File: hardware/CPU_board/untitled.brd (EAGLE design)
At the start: 128.9 x 94.9 mm, 67 parts, among them IC1 MAX232ECWE, IC2 MAX232ECWE, IC3 AM29F040J, IC4 74HCT138D, IC5 LM2596S, IC6 74245SSOP, IC7 74245SSOP, IC8 74245SSOP, J2 POWER_JACKSLT, U1 AS6C4008-55SIN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

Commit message: Power trace updated
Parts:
- moved IC6 1.91 mm to (54.1, 53.3)
- moved C1 1.30 mm to (51.1, 23.5)
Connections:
- removed net VCC: IC7.20, IC8.20
- net 5V: now also IC7.20, IC8.20
- net GND: now also IC8.19, IC8.2, IC8.3, IC8.4, IC8.5
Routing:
- net 5V: track 382.6 -> 414.0 mm, vias 10 -> 9
- net GND: track 89.3 -> 94.2 mm, vias 27 -> 30
- net !RST: track 168.4 -> 165.1 mm, vias 1 -> 3
- net PD7_IN: track 9.88 -> 11.8 mm
- net PD6_IN: track 10.1 -> 12.0 mm
- net PD5_IN: track 10.2 -> 12.1 mm
- net PD4_IN: track 10.2 -> 12.1 mm
- net PD3_IN: track 10.3 -> 12.2 mm
- net PD2_IN: track 10.3 -> 12.3 mm
- net PD1_IN: track 10.4 -> 12.3 mm
- net PD0_IN: track 10.5 -> 12.4 mm
- net PR_OUT2: track 29.4 -> 28.2 mm
- net PR_OUT4: track 31.2 -> 30.1 mm
- net PR_OUT3: track 30.3 -> 29.2 mm
- net PR_OUT1: track 28.4 -> 27.3 mm
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
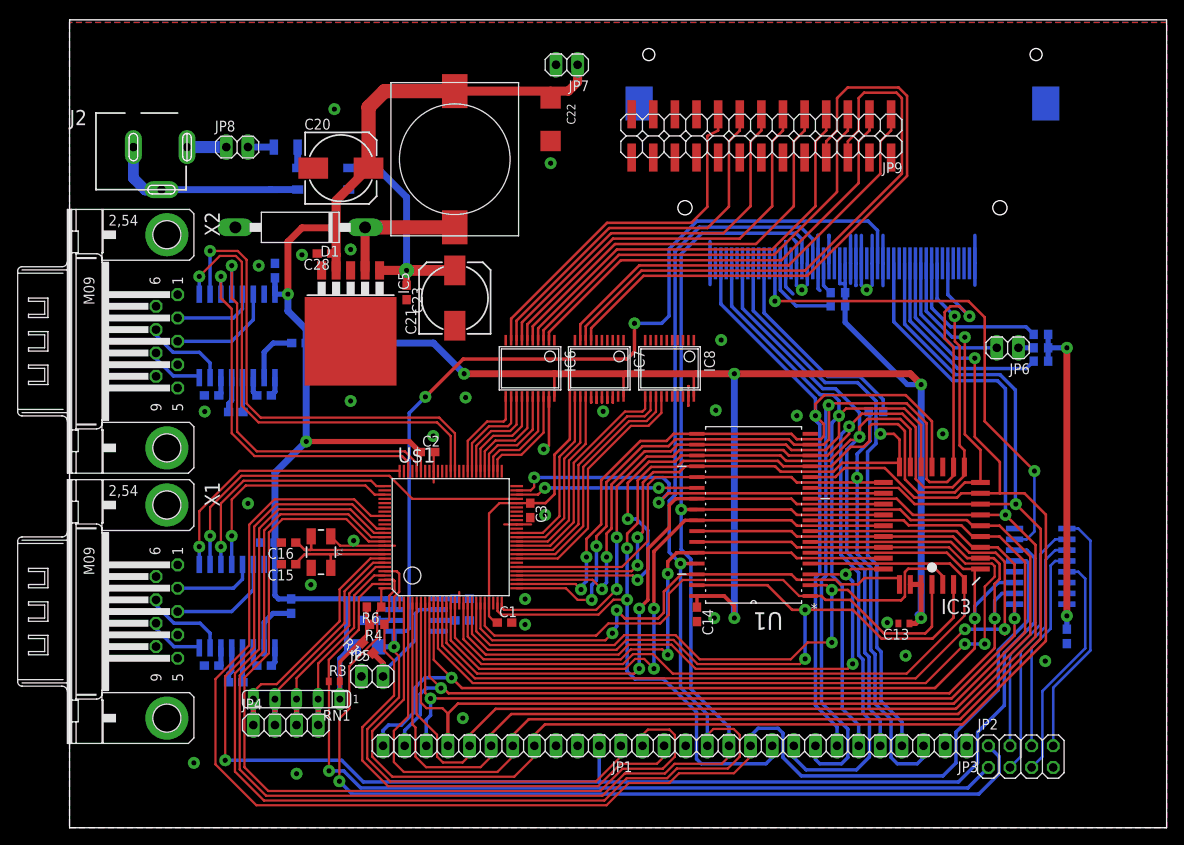
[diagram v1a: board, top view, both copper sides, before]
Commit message: VCC rerouted
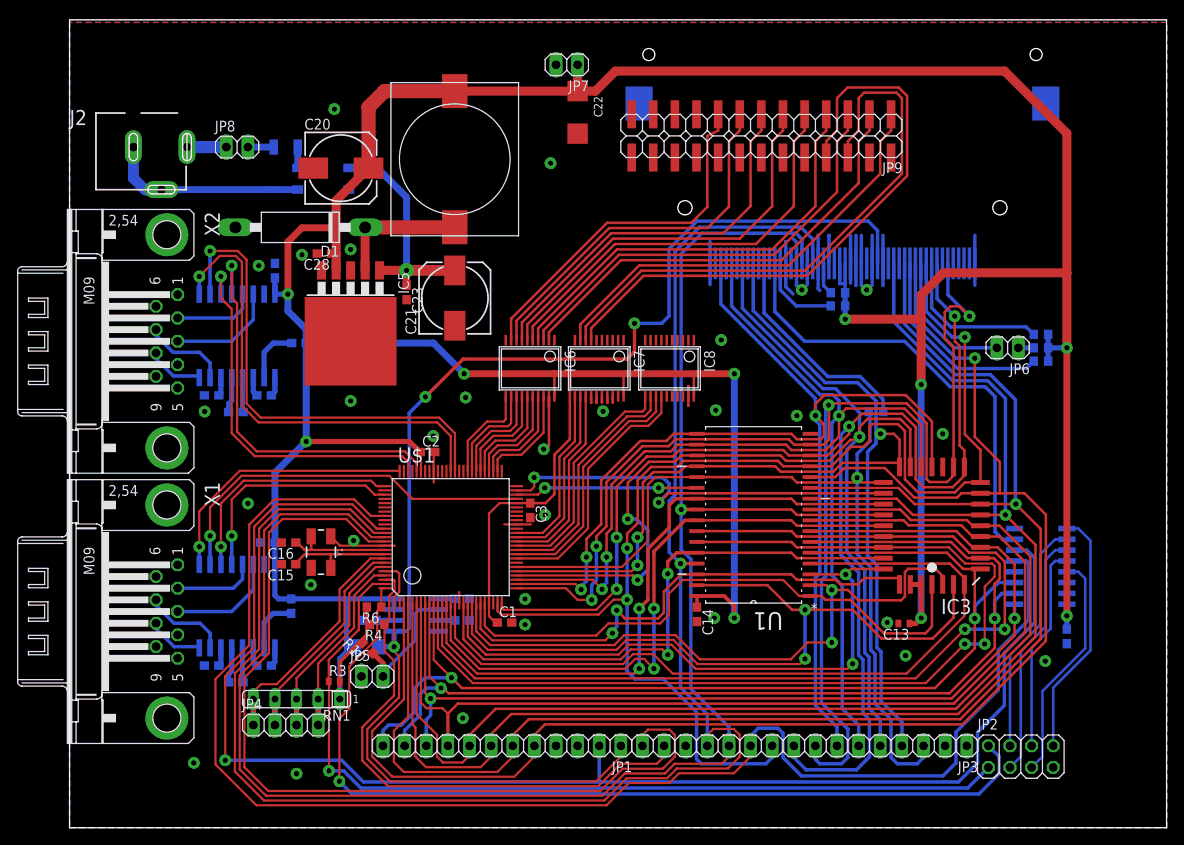
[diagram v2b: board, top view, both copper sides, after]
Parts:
- moved C22 3.29 mm to (59.7, 83.4)
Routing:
- net 5V: track 414.0 -> 502.8 mm, vias 9 -> 10
- net CF_CS0: track 60.2 -> 54.2 mm, vias 2 -> 0
- net A2: track 177.0 -> 176.3 mm
- net A1: track 182.6 -> 181.9 mm
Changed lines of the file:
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@@
 <element name="L2" library="mw" package="NIX_CHOKE_SMD" value="NIX_CHOKE_SMD" x="52.7558" y="68.9102" rot="R90"/>
 <element name="JP7" library="pinhead" package="1X02" value="" x="58.42" y="89.0016" rot="R180"/>
-<element name="C22" library="rcl" package="SMC_C" value="" x="56.515" y="82.55" rot="R270"/>
+<element name="C22" library="rcl" package="SMC_C" value="" x="59.69" y="83.4136" rot="R270"/>
 <element name="JP8" library="pinhead" package="1X02" value="" x="19.685" y="79.335"/>
 <element name="JP9" library="pinhead-2" package="2X13SMD" value="" x="95.25" y="79.375" rot="R180"/>
@@
 <via x="78.105" y="52.705" extent="1-16" drill="0.6" diameter="1.4224" shape="octagon"/>
 <contactref element="IC4" pad="16"/>
-<wire x1="99.6696" y1="24.384" x2="100.0506" y2="24.003" width="0.8128" layer="16"/>
 <wire x1="98.678759375" y1="23.368" x2="99.4156" y2="23.368" width="0.6096" layer="1"/>
 <wire x1="99.4156" y1="23.368" x2="100.0506" y2="24.003" width="0.6096" layer="1"/>
@@
 <contactref element="R5" pad="2"/>
 <wire x1="100.0506" y1="24.003" x2="100.0506" y2="51.435" width="0.8128" layer="16"/>
-<wire x1="78.105" y1="52.705" x2="98.7806" y2="52.705" width="0.8128" layer="1"/>
-<wire x1="98.7806" y1="52.705" x2="100.0506" y2="51.435" width="0.8128" layer="1"/>
 <wire x1="90.4875" y1="65.675" x2="90.4875" y2="63.2968" width="0.4064" layer="16"/>
 <wire x1="90.4875" y1="63.2968" x2="91.1225" y2="63.2968" width="0.4064" layer="16"/>
@@
 <wire x1="91.1225" y1="62.2309" x2="91.1225" y2="60.6815" width="0.6096" layer="16"/>
 <wire x1="91.1225" y1="60.6815" x2="91.1216" y2="60.6806" width="0.6096" layer="16"/>
-<wire x1="91.1216" y1="60.6806" x2="91.1216" y2="58.7384" width="0.6096" layer="16"/>
-<wire x1="91.1216" y1="58.7384" x2="98.425" y2="51.435" width="0.6096" layer="16"/>
-<wire x1="100.0506" y1="51.435" x2="98.425" y2="51.435" width="0.6096" layer="16"/>
+<wire x1="91.1216" y1="60.6806" x2="91.1216" y2="59.1194" width="0.6096" layer="16"/>
 <wire x1="114.9722" y1="54.1782" x2="114.9722" y2="55.753" width="0.6096" layer="16"/>
 <wire x1="114.9722" y1="55.753" x2="114.9722" y2="57.3278" width="0.6096" layer="16"/>
@@
 <wire x1="27.305" y1="69.85" x2="31.3182" y2="69.85" width="0.8128" layer="1"/>
 <contactref element="JP7" pad="1"/>
-<wire x1="45.2558" y1="85.9102" x2="56.515" y2="85.9102" width="1.0668" layer="1"/>
-<wire x1="56.515" y1="85.9102" x2="58.6052" y2="85.9102" width="1.0668" layer="1"/>
-<wire x1="58.6052" y1="85.9102" x2="59.69" y2="86.995" width="1.0668" layer="1"/>
-<wire x1="59.69" y1="86.995" x2="59.69" y2="89.0016" width="1.0668" layer="1"/>
+<wire x1="45.2558" y1="85.9102" x2="59.69" y2="85.9102" width="1.0668" layer="1"/>
+<wire x1="59.69" y1="85.9102" x2="59.69" y2="89.0016" width="1.0668" layer="1"/>
 <contactref element="C22" pad="+"/>
-<wire x1="56.515" y1="85.05" x2="56.515" y2="85.9102" width="0.6096" layer="1"/>
 <wire x1="27.7994" y1="56.3118" x2="27.7994" y2="44.7412" width="0.8128" layer="16"/>
 <wire x1="24.13" y1="41.0718" x2="27.7994" y2="44.7412" width="0.8128" layer="16"/>
@@
 <wire x1="39.9424" y1="44.7412" x2="41.1734" y2="43.5102" width="0.6096" layer="1"/>
 <wire x1="41.2124" y1="43.5102" x2="41.1734" y2="43.5102" width="0.6096" layer="1"/>
-<wire x1="100.0506" y1="51.435" x2="114.9722" y2="54.1782" width="0" layer="19" extent="16-16"/>
+<via x="91.1216" y="59.1194" extent="1-16" drill="0.6" diameter="1.4224" shape="octagon"/>
+<wire x1="59.69" y1="85.9102" x2="61.7802" y2="85.9102" width="1.0668" layer="1"/>
+<wire x1="61.7802" y1="85.9102" x2="64.135" y2="88.265" width="1.0668" layer="1"/>
+<wire x1="64.135" y1="88.265" x2="109.855" y2="88.265" width="1.0668" layer="1"/>
+<wire x1="109.855" y1="88.265" x2="117.1702" y2="80.9498" width="1.0668" layer="1"/>
+<wire x1="117.1702" y1="55.753" x2="117.1702" y2="64.56524375" width="1.0668" layer="1"/>
+<wire x1="117.1702" y1="64.56524375" x2="117.1702" y2="80.9498" width="1.0668" layer="1"/>
+<wire x1="91.1216" y1="59.1194" x2="100.0506" y2="59.1194" width="1.0668" layer="1"/>
+<wire x1="100.0506" y1="59.1194" x2="100.0506" y2="51.435" width="1.0668" layer="1"/>
+<wire x1="117.1702" y1="64.56524375" x2="102.66524375" y2="64.56524375" width="1.0668" layer="1"/>
+<wire x1="102.66524375" y1="64.56524375" x2="100.0506" y2="61.9506" width="1.0668" layer="1"/>
+<wire x1="100.0506" y1="59.1194" x2="100.0506" y2="61.9506" width="1.0668" layer="1"/>
+<wire x1="59.69" y1="85.9102" x2="59.69" y2="85.9136" width="0" layer="19" extent="1-1"/>
 <wire x1="59.69" y1="8.9916" x2="50.2548" y2="23.4696" width="0" layer="19" extent="1-1"/>
 </signal>
@@
 <via x="111.1758" y="37.3888" extent="1-16" drill="0.6" diameter="1.4224" shape="octagon"/>
 <wire x1="114.0968" y1="34.4678" x2="111.1758" y2="37.3888" width="0.3048" layer="1"/>
-<wire x1="111.125" y1="50.8" x2="111.125" y2="37.4396" width="0.4064" layer="16"/>
+<wire x1="111.125" y1="49.657" x2="111.125" y2="37.4396" width="0.4064" layer="16"/>
 <wire x1="111.125" y1="37.4396" x2="111.1758" y2="37.3888" width="0.4064" layer="16"/>
 <wire x1="98.1075" y1="58.5343" x2="104.0384" y2="52.6034" width="0.4064" layer="16"/>
-<wire x1="104.0384" y1="52.6034" x2="109.3216" y2="52.6034" width="0.4064" layer="16"/>
-<wire x1="109.3216" y1="52.6034" x2="111.125" y2="50.8" width="0.4064" layer="16"/>
+<wire x1="104.0384" y1="52.6034" x2="108.1786" y2="52.6034" width="0.4064" layer="16"/>
+<wire x1="111.125" y1="49.657" x2="108.1786" y2="52.6034" width="0.4064" layer="16"/>
 </signal>
 <signal name="A2">
@@
 <via x="109.9566" y="36.1188" extent="1-16" drill="0.6" diameter="1.4224" shape="octagon"/>
 <wire x1="113.4872" y1="32.5882" x2="109.9566" y2="36.1188" width="0.3048" layer="1"/>
-<wire x1="109.9566" y1="36.1188" x2="109.9566" y2="50.9524" width="0.4064" layer="16"/>
+<wire x1="109.9566" y1="36.1188" x2="109.9566" y2="49.8094" width="0.4064" layer="16"/>
 <wire x1="96.8375" y1="65.675" x2="96.8375" y2="58.8137" width="0.4064" layer="16"/>
 <wire x1="96.8375" y1="58.8137" x2="103.759" y2="51.8922" width="0.4064" layer="16"/>
-<wire x1="103.759" y1="51.8922" x2="109.0168" y2="51.8922" width="0.4064" layer="16"/>
-<wire x1="109.0168" y1="51.8922" x2="109.9566" y2="50.9524" width="0.4064" layer="16"/>
+<wire x1="103.759" y1="51.8922" x2="107.8738" y2="51.8922" width="0.4064" layer="16"/>
+<wire x1="109.9566" y1="49.8094" x2="107.8738" y2="51.8922" width="0.4064" layer="16"/>
 </signal>
 <signal name="A3">
@@
 <signal name="CF_CS0">
 <contactref element="CON1" pad="7"/>
-<wire x1="82.8675" y1="65.675" x2="82.8675" y2="61.2394" width="0.4064" layer="16"/>
-<via x="82.8675" y="61.2394" extent="1-16" drill="0.6" diameter="1.4224" shape="octagon"/>
-<via x="113.3602" y="41.275" extent="1-16" drill="0.6" diameter="1.4224" shape="octagon"/>
-<wire x1="107.5182" y1="47.117" x2="113.3602" y2="41.275" width="0.3048" layer="1"/>
-<wire x1="107.5182" y1="59.3344" x2="107.5182" y2="47.117" width="0.3048" layer="1"/>
+<wire x1="82.8675" y1="65.675" x2="82.8675" y2="60.0075" width="0.4064" layer="16"/>
 <contactref element="IC4" pad="7"/>
-<wire x1="113.3602" y1="41.275" x2="113.3602" y2="34.163" width="0.3048" layer="16"/>
-<wire x1="113.3602" y1="34.163" x2="112.4458" y2="33.2486" width="0.3048" layer="16"/>
-<wire x1="112.4458" y1="33.2486" x2="111.0234" y2="33.2486" width="0.3048" layer="16"/>
-<wire x1="107.5182" y1="59.3344" x2="105.6132" y2="61.2394" width="0.3048" layer="1"/>
-<wire x1="82.8675" y1="61.2394" x2="105.6132" y2="61.2394" width="0.3048" layer="1"/>
+<wire x1="111.0234" y1="33.2486" x2="109.6264" y2="33.2486" width="0.4064" layer="16"/>
+<wire x1="109.6264" y1="33.2486" x2="108.7374" y2="34.1376" width="0.4064" layer="16"/>
+<wire x1="108.7374" y1="34.1376" x2="108.7374" y2="50.0126" width="0.4064" layer="16"/>
+<wire x1="108.7374" y1="50.0126" x2="107.569" y2="51.181" width="0.4064" layer="16"/>
+<wire x1="107.569" y1="51.181" x2="103.4542" y2="51.181" width="0.4064" layer="16"/>
+<wire x1="103.4542" y1="51.181" x2="98.1202" y2="56.515" width="0.4064" layer="16"/>
+<wire x1="82.8675" y1="60.0075" x2="86.36" y2="56.515" width="0.4064" layer="16"/>
+<wire x1="86.36" y1="56.515" x2="98.1202" y2="56.515" width="0.4064" layer="16"/>
 </signal>
 <signal name="N$31">
